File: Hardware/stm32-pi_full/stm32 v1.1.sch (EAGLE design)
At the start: 288 parts, among them IC2 AD8519KS, J1 JUMPER-SMT_2_NC_TRACE_NO-SILK, Q1 PNP, Q2 NPN, Q3 NPN, U1 ESP32-WROOM-32D

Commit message: commit
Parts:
- removed FB6: (no value), microbuilder:FERRITE_0603
- removed SJ1: JUMPER-SMT_2_NC_TRACE_NO-SILK, SparkFun-Jumpers:JUMPER-SMT_2_NC_TRACE_NO-SILK
- removed SJ2: JUMPER-SMT_2_NO_SILK, SparkFun-Jumpers:JUMPER-SMT_2_NO_SILK
- added TP12: TEST-POINT3, SparkFun-Connectors:TEST-POINT3
- C11: value 22uF -> 1uF
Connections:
- removed net +5V_REF: C11.1, C37.1, FB6.P$1, REF19X.!SHDN, REF19X.VIN, TP11.1
- removed net N$12: REF19X.GND, SJ1.2, SJ2.2, TP10.1
- net +3V3ANA: now also C11.1, C37.1, REF19X.!SHDN, REF19X.VIN, TP11.1
- net +5V: no longer FB6.P$2
- net AGND: now also C11.2, C37.2, REF19X.GND, TP10.1; no longer SJ1.1
- net DGND: no longer C11.2, C37.2, SJ2.1
- net VBAT: now also TP12.1

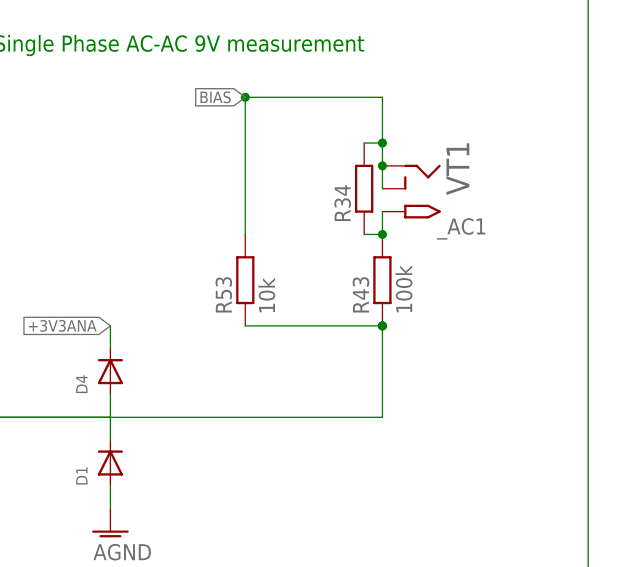
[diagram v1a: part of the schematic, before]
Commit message: update ac-ac resistor value for new vref
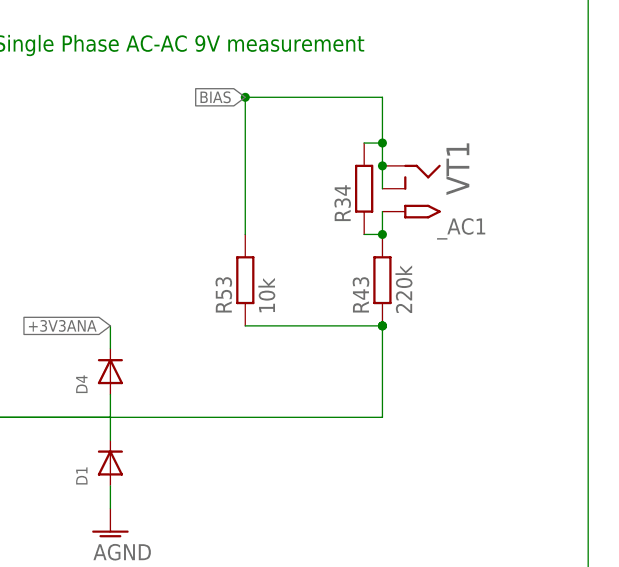
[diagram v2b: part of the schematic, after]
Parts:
- R43: value 100k -> 220k
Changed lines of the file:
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@@
 <drawing>
 <settings>
-<setting alwaysvectorfont="yes"/>
+<setting alwaysvectorfont="no"/>
 <setting keepoldvectorfont="yes"/>
 <setting verticaltext="up"/>
@@
 <part name="RJ1" library="95501-6889 rj45 smt" deviceset="95501-6889" device="" value="95501-6889"/>
 <part name="STM32F303VE" library="stm32f303" deviceset="STM32F303XB" device="" value="STM32F303VE"/>
-<part name="R43" library="resistor" deviceset="R-EU_" device="R0603" value="100k"/>
+<part name="R43" library="resistor" deviceset="R-EU_" device="R0603" value="220k"/>
 <part name="CV2" library="rcl" library_urn="urn:adsk.eagle:library:334" deviceset="C-EU" device="C0805" package3d_urn="urn:adsk.eagle:package:23617/2" value="10nF 5%"/>
 <part name="CV1" library="rcl" library_urn="urn:adsk.eagle:library:334" deviceset="C-EU" device="C0805" package3d_urn="urn:adsk.eagle:package:23617/2" value="10nF 5%"/>
